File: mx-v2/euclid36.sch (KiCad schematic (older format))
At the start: 115 parts, among them SW1 RotaryEncoder_Switch, SW10 SW_PUSH, SW11 SW_PUSH, SW12 SW_PUSH, SW14 SW_PUSH, SW15 SW_PUSH, SW16 SW_PUSH, SW17 SW_PUSH, SW18 SW_PUSH, SW19 SW_PUSH, SW2 SW_PUSH, SW20 SW_PUSH, SW21 SW_PUSH, SW22 SW_PUSH, SW23 SW_PUSH, SW25 SW_PUSH, SW26 SW_PUSH, SW27 SW_PUSH, SW28 SW_PUSH, SW29 SW_PUSH, SW3 SW_PUSH, SW31 SW_PUSH, SW32 SW_PUSH, SW33 SW_PUSH, SW34 SW_PUSH, SW35 SW_PUSH, SW37 SW_PUSH, SW38 SW_PUSH, SW39 SW_PUSH, SW4 SW_PUSH, SW40 SW_PUSH, SW41 SW_PUSH, SW42 SW_PUSH, SW5 SW_PUSH, SW6 SW_PUSH, SW7 RotaryEncoder_Switch, SW8 SW_PUSH, SW9 SW_PUSH, U1 USBLC6-2SC6, U2 ATmega32U4-AU, Y1 XTAL

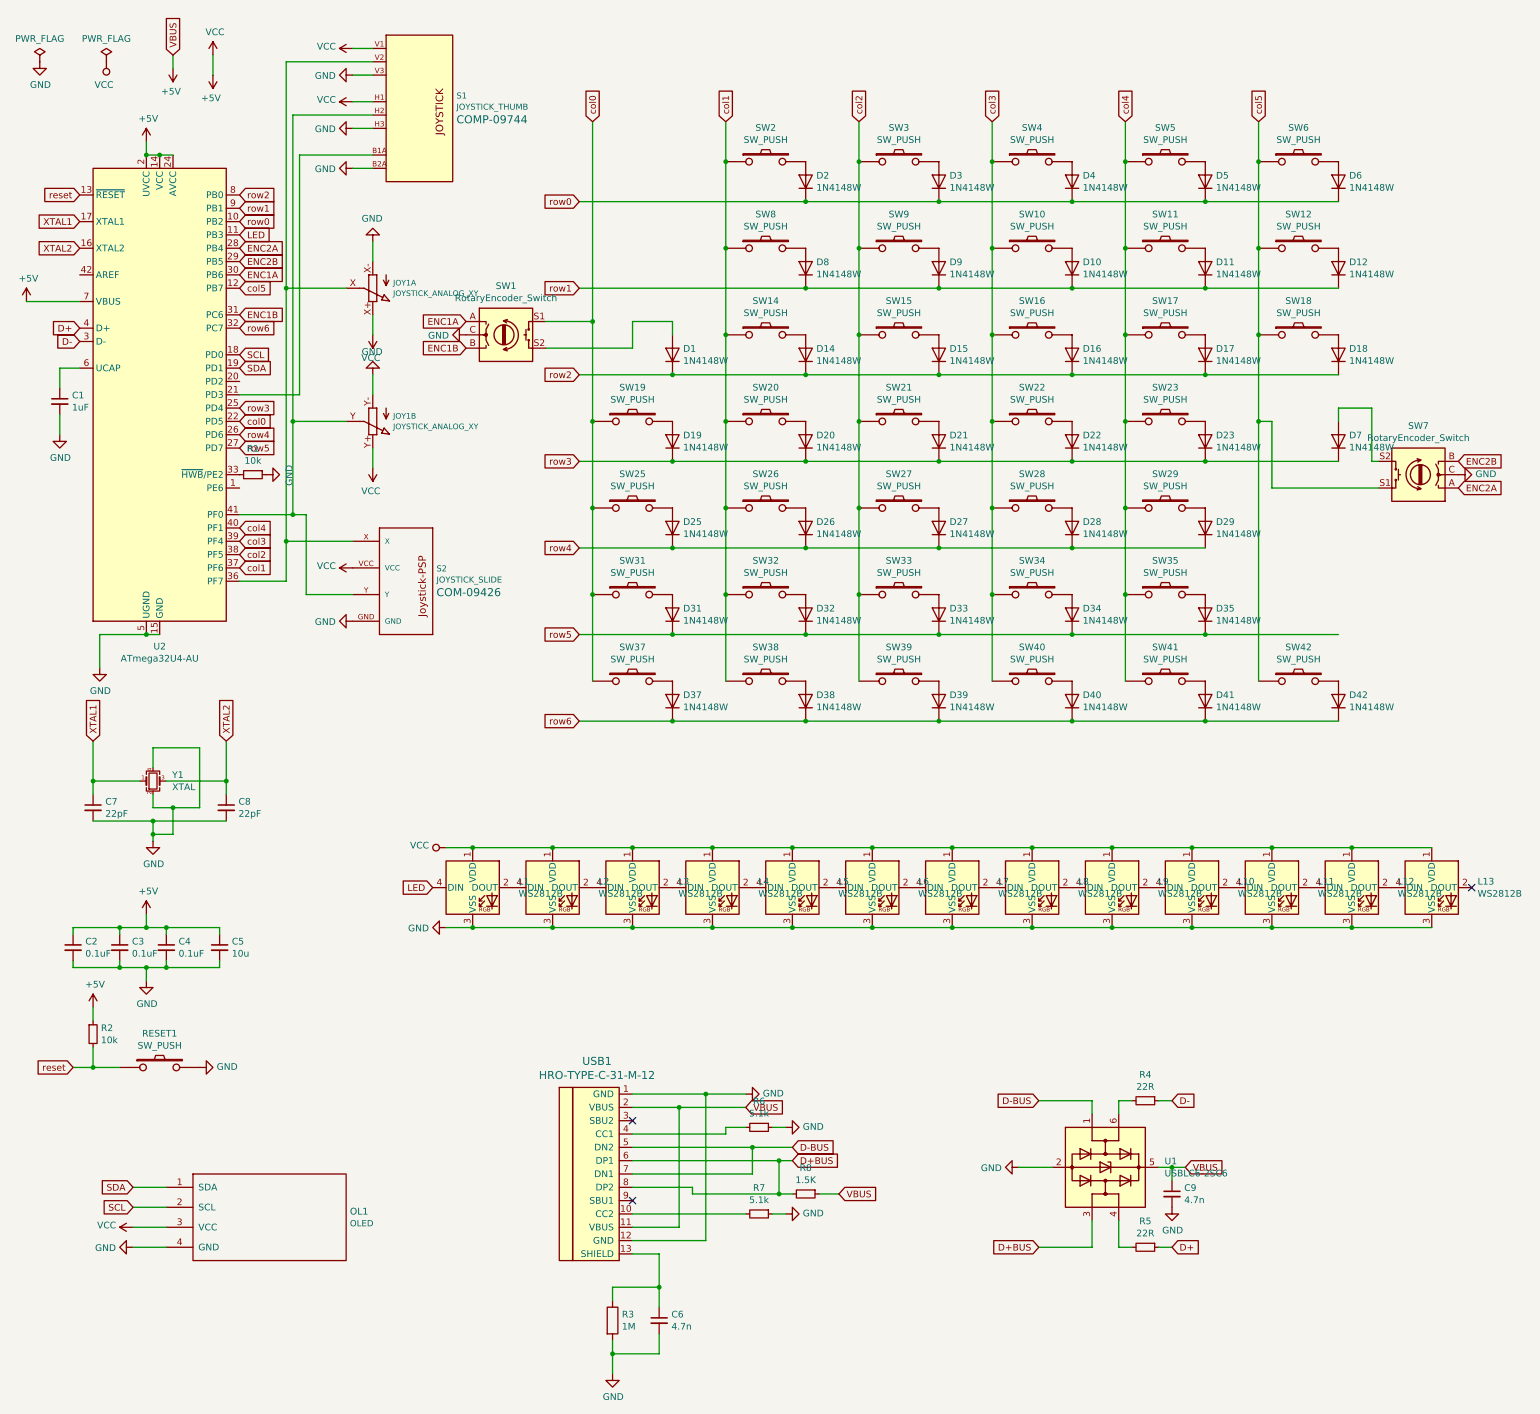
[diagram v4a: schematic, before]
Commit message: added verbiage to ask people to share builds and pictures with me
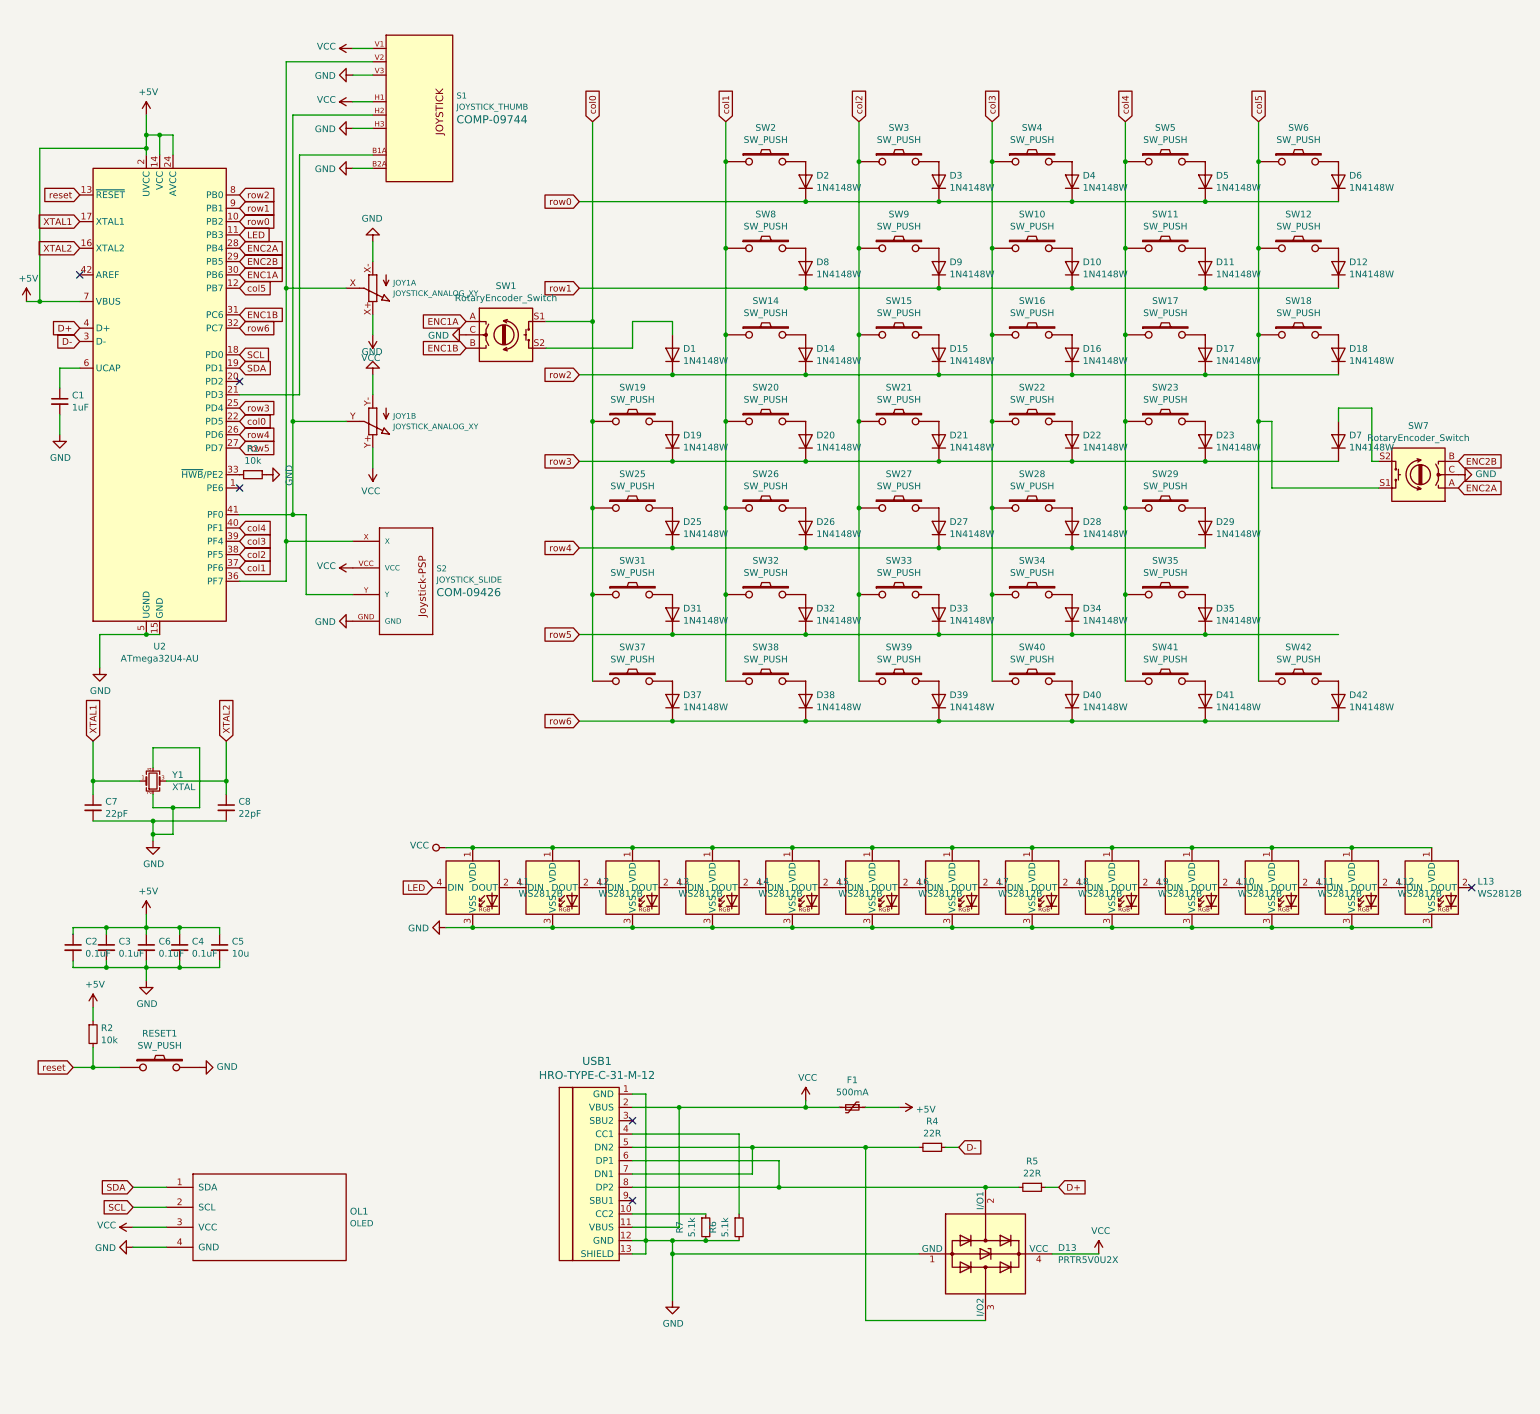
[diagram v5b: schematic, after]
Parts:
- removed C9: 4.7n, Capacitor_SMD:C_0805_2012Metric, symbol Device:C_Small
- removed R3: 1M, Resistor_SMD:R_0805_2012Metric, symbol Device:R
- removed R8: 1.5K, Resistor_SMD:R_0805_2012Metric, symbol Device:R_Small
- removed U1: USBLC6-2SC6, Package_TO_SOT_SMD:SOT-23-6, symbol Power_Protection:USBLC6-2SC6
- added D13: PRTR5V0U2X, Package_TO_SOT_SMD:SOT-143, symbol Power_Protection:PRTR5V0U2X
- added F1: 500mA, Fuse:Fuse_1206_3216Metric_Pad1.42x1.75mm_HandSolder, symbol Device:Polyfuse_Small
- C6: value 4.7n -> 0.1uF; footprint Capacitor_SMD:C_0805_2012Metric -> Capacitor_SMD:C_0805_2012Metric_Pad1.18x1.45mm_HandSolder; LCSC C50131 -> C49678
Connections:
- net D+BUS is gone; now on an unnamed net: USB1.6 (DP1), USB1.8 (DP2)
- net D-BUS is gone; now on an unnamed net: USB1.5 (DN2), USB1.7 (DN1)
- net +5V: now also C6.1, F1.1; no longer JOY1.X+ (E), JOY1.Y+ (E), L1.1 (VDD), L10.1 (VDD), L11.1 (VDD), L12.1 (VDD), L13.1 (VDD), L2.1 (VDD), L3.1 (VDD), L4.1 (VDD), L5.1 (VDD), L6.1 (VDD), L7.1 (VDD), L8.1 (VDD), L9.1 (VDD), OL1.3 (VCC), S1.H1 (H+), S1.V1 (V+), S2.VCC, USB1.11 (VBUS), USB1.2 (VBUS)
- net GND: now also R6.2, R7.2, USB1.13 (SHIELD), D13.1 (GND); no longer R6.1, R7.1
- net at USB1.10 (CC2): now also R7.1; no longer R7.2
- net at USB1.4 (CC1): now also R6.1; no longer R6.2
- net at R5.2: now also D13.2 (I/O1)
- net at R4.2: now also D13.3 (I/O2)
- new net VCC: D13.4 (VCC), F1.2, JOY1.X+ (E), JOY1.Y+ (E), L1.1 (VDD), L10.1 (VDD), L11.1 (VDD), L12.1 (VDD), L13.1 (VDD), L2.1 (VDD), L3.1 (VDD), L4.1 (VDD), L5.1 (VDD), L6.1 (VDD), L7.1 (VDD), L8.1 (VDD), L9.1 (VDD), OL1.3 (VCC), S1.H1 (H+), S1.V1 (V+), S2.VCC, USB1.11 (VBUS), USB1.2 (VBUS)
- no-connect marks 3 -> 6
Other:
- moved on the sheet: C3, C4, R4, R5, R6, R7
